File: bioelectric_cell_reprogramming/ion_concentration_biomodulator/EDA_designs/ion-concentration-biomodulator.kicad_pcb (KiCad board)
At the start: 4 copper layers, 87.5 x 87.5 mm, 53 parts, among them J1 532610671, J10 39-53-2045, J11 Conn_01x14_Pin, J12 Conn_01x14_Pin, J13 39-53-2045, J14 39-53-2045, J15 Conn_ARM_SWD_TagConnect_TC2030, J16 IPL1-104-01-L-D-K, J17 Conn_01x02_Pin, J18 EJ508A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

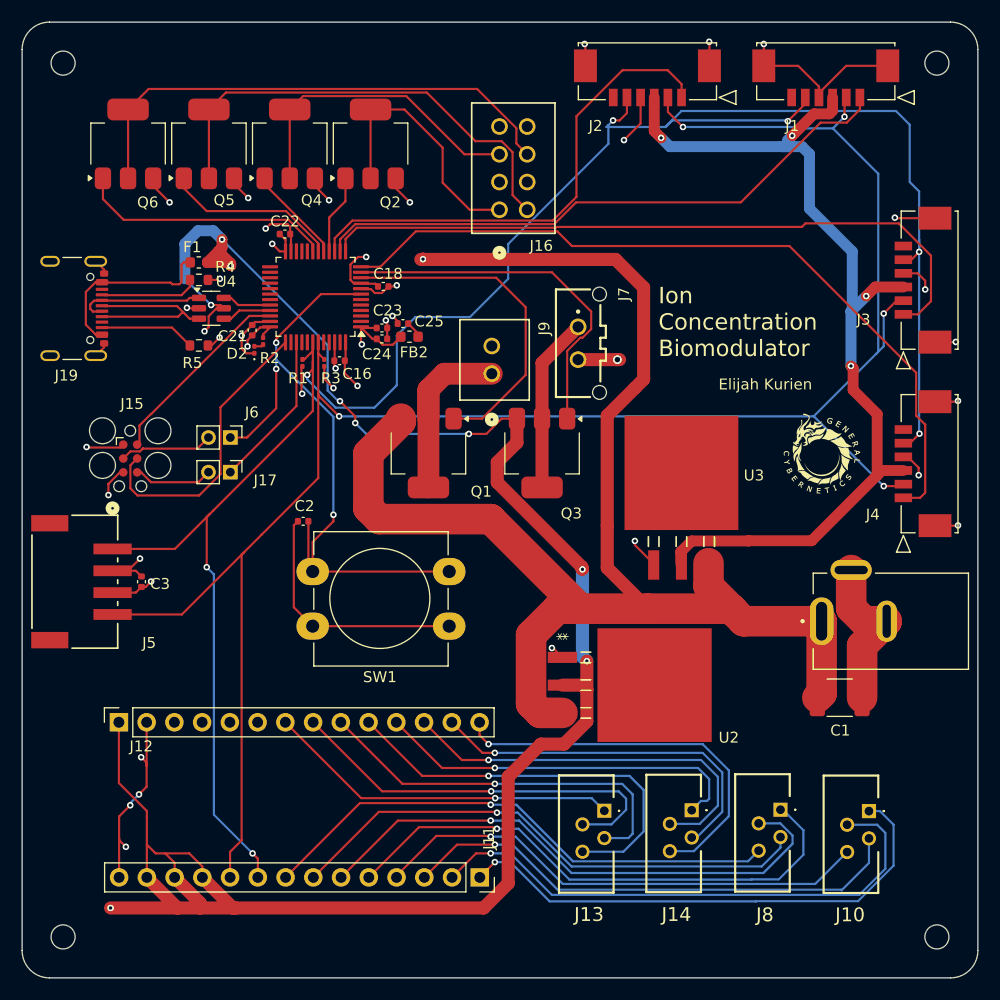
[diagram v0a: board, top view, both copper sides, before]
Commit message: fix(icbm): update tolerances to comply with new dru
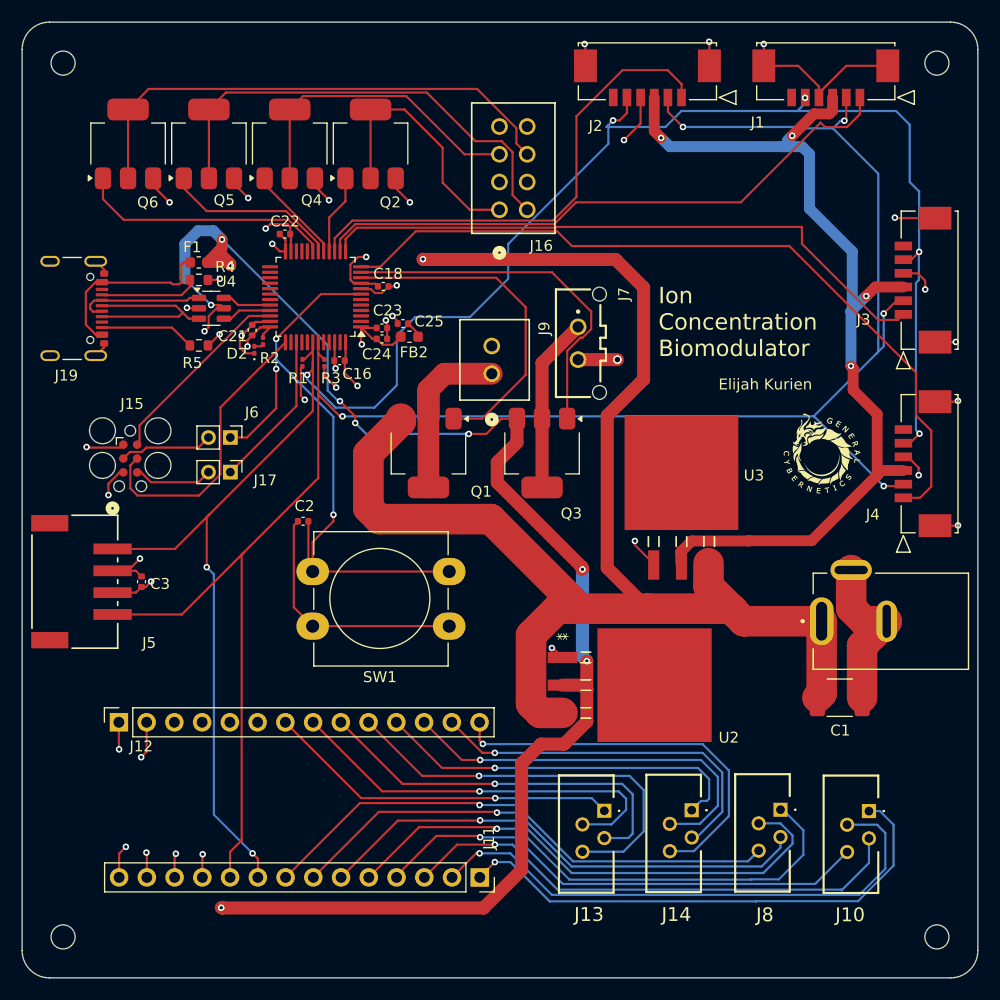
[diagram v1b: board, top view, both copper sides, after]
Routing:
- net +5V: track 187.3 -> 149.7 mm, vias 10 -> 14
- net /I2C_SCK: track 192.7 -> 179.0 mm
- net GND: track 139.4 -> 127.7 mm, vias 28 -> 26
- net /IRQn2: track 63.7 -> 57.3 mm
- net Net-(Q3-D): track 17.1 -> 16.1 mm
- net +3.3V: track 126.1 -> 126.9 mm
- net /IRQn3: track 54.7 -> 55.3 mm
- added copper zone on In2.Cu, net +12V
- added copper zone on In2.Cu, net +3.3V
- added copper zone on In2.Cu, net +5V
- added copper zone on In1.Cu, net GND
- removed copper zone on In1.Cu, net +12V
- removed copper zone on In1.Cu, net +3.3V
- removed copper zone on In1.Cu, net +5V
- removed copper zone on In2.Cu, net GND

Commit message: refactor(icbm): improve capacitor placement
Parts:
- moved C2 7.27 mm to (124.5, 102.0), turned to -90 degrees
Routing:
- net GND: track 127.7 -> 120.6 mm
- net /NRST: track 60.7 -> 64.1 mm
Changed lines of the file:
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@@
 	(footprint "Capacitor_SMD:C_0402_1005Metric"
 		(layer "F.Cu")
-		(at 126.201002 94.971002 180)
+		(at 124.55 102.05 -90)
 		(descr "Capacitor SMD 0402 (1005 Metric), square (rectangular) end terminal, IPC_7351 nominal, (Body size source: IPC-SM-782 page 76, https://www.pcb-3d.com/wordpress/wp-content/uploads/ipc-sm-782a_amendment_1_and_2.pdf), generated with kicad-footprint-generator")
 		(tags "capacitor")
 		(property "Reference" "C2"
-			(at -0.12 1.4 180)
+			(at -0.12 1.4 90)
 			(layer "F.SilkS")
 			(effects
@@
 		)
 		(property "Value" "100nF"
-			(at 0 1.16 180)
+			(at 0 1.16 90)
 			(layer "F.Fab")
 			(effects
@@
 		)
 		(property "Footprint" "Capacitor_SMD:C_0402_1005Metric"
-			(at 0 0 180)
+			(at 0 0 -90)
 			(unlocked yes)
 			(layer "F.Fab")
@@
 		)
 		(property "Datasheet" ""
-			(at 0 0 180)
+			(at 0 0 -90)
 			(unlocked yes)
 			(layer "F.Fab")
@@
 		)
 		(property "Description" "Unpolarized capacitor"
-			(at 0 0 180)
+			(at 0 0 -90)
 			(unlocked yes)
 			(layer "F.Fab")
@@
 		)
 		(fp_line
-			(start 0.91 0.46)
-			(end -0.91 0.46)
+			(start -0.91 0.46)
+			(end -0.91 -0.46)
 			(stroke
 				(width 0.05)
@@
 		)
 		(fp_line
-			(start 0.91 -0.46)
-			(end 0.91 0.46)
+			(start 0.91 0.46)
+			(end -0.91 0.46)
 			(stroke
 				(width 0.05)
@@
 		)
 		(fp_line
-			(start -0.91 0.46)
-			(end -0.91 -0.46)
+			(start -0.91 -0.46)
+			(end 0.91 -0.46)
 			(stroke
 				(width 0.05)
@@
 		)
 		(fp_line
-			(start -0.91 -0.46)
-			(end 0.91 -0.46)
+			(start 0.91 -0.46)
+			(end 0.91 0.46)
 			(stroke
 				(width 0.05)
@@
 		)
 		(fp_line
-			(start 0.5 0.25)
-			(end -0.5 0.25)
+			(start -0.5 0.25)
+			(end -0.5 -0.25)
 			(stroke
 				(width 0.1)
@@
 		)
 		(fp_line
-			(start 0.5 -0.25)
-			(end 0.5 0.25)
+			(start 0.5 0.25)
+			(end -0.5 0.25)
 			(stroke
 				(width 0.1)
@@
 		)
 		(fp_line
-			(start -0.5 0.25)
-			(end -0.5 -0.25)
+			(start -0.5 -0.25)
+			(end 0.5 -0.25)
 			(stroke
 				(width 0.1)
@@
 		)
 		(fp_line
-			(start -0.5 -0.25)
-			(end 0.5 -0.25)
+			(start 0.5 -0.25)
+			(end 0.5 0.25)
 			(stroke
 				(width 0.1)
@@
 		)
 		(fp_text user "${REFERENCE}"
-			(at 0 0 180)
+			(at 0 0 90)
 			(layer "F.Fab")
 			(effects
@@
 		)
 		(pad "1" smd roundrect
-			(at -0.48 0 180)
+			(at -0.48 0 270)
 			(size 0.56 0.62)
 			(layers "F.Cu" "F.Paste" "F.Mask")
@@
 		)
 		(pad "2" smd roundrect
-			(at 0.48 0 180)
+			(at 0.48 0 270)
 			(size 0.56 0.62)
 			(layers "F.Cu" "F.Paste" "F.Mask")
@@
 	)
 	(segment
-		(start 125.344002 102.844002)
-		(end 127.071002 104.571002)
-		(width 0.2)
-		(layer "F.Cu")
-		(net 2)
-	)
-	(segment
 		(start 109.733502 90.491002)
 		(end 109.408998 90.491002)
@@
 	)
 	(segment
+		(start 127.071002 104.571002)
+		(end 125.03 102.53)
+		(width 0.2)
+		(layer "F.Cu")
+		(net 2)
+	)
+	(segment
 		(start 129.053502 80.853502)
 		(end 129.171002 80.971002)
@@
 	)
 	(segment
-		(start 125.721002 94.971002)
-		(end 125.344002 95.348002)
-		(width 0.2)
-		(layer "F.Cu")
-		(net 2)
-	)
-	(segment
 		(start 129.053502 80.271002)
 		(end 129.053502 80.853502)
@@
 	)
 	(segment
-		(start 125.344002 95.348002)
-		(end 125.344002 102.844002)
-		(width 0.2)
-		(layer "F.Cu")
-		(net 2)
-	)
-	(segment
 		(start 181.55 89.071002)
 		(end 182.55 90.071002)
@@
 	)
 	(segment
+		(start 125.03 102.53)
+		(end 124.55 102.53)
+		(width 0.2)
+		(layer "F.Cu")
+		(net 2)
+	)
+	(segment
 		(start 108.75 99.5)
 		(end 110.879998 99.5)
@@
 	)
 	(segment
+		(start 125.072004 101.57)
+		(end 124.55 101.57)
+		(width 0.2)
+		(layer "F.Cu")
+		(net 3)
+	)
+	(segment
 		(start 126.681002 99.181002)
 		(end 127.071002 99.571002)
@@
 		(width 0.2)
 		(layer "F.Cu")
+		(net 3)
+	)
+	(segment
+		(start 127.071002 99.571002)
+		(end 125.072004 101.57)
+		(width 0.2)
+		(layer "F.Cu")

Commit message: Testing add_project_libraries.sh
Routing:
- net /NRST: track 64.1 -> 59.9 mm
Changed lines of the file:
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@@
-	)
-	(segment
-		(start 126.681002 94.971002)
-		(end 126.681002 99.181002)
-		(width 0.2)
-		(layer "F.Cu")
-		(net 3)
 	)
 	(segment
